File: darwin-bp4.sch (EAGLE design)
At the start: 21 parts, among them U1 MCP23008, U2 TCA9548A, U3 LP5012

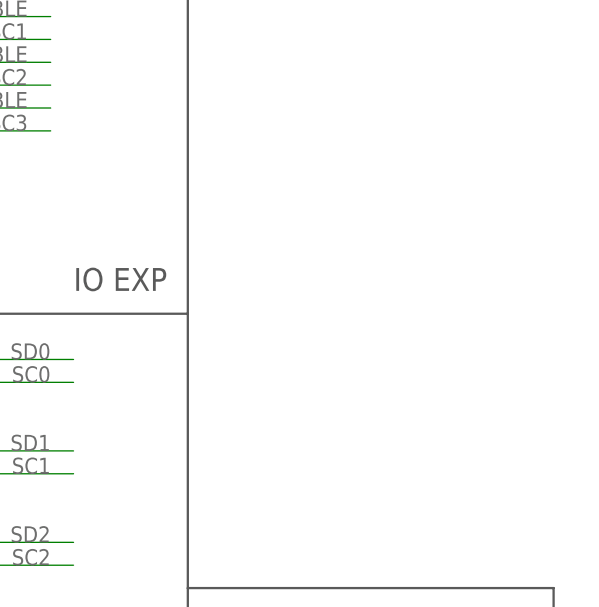
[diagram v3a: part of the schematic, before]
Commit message: Fixed power to LED controller, added pulldowns on hot swap detection pins, adjusted standoff holes.
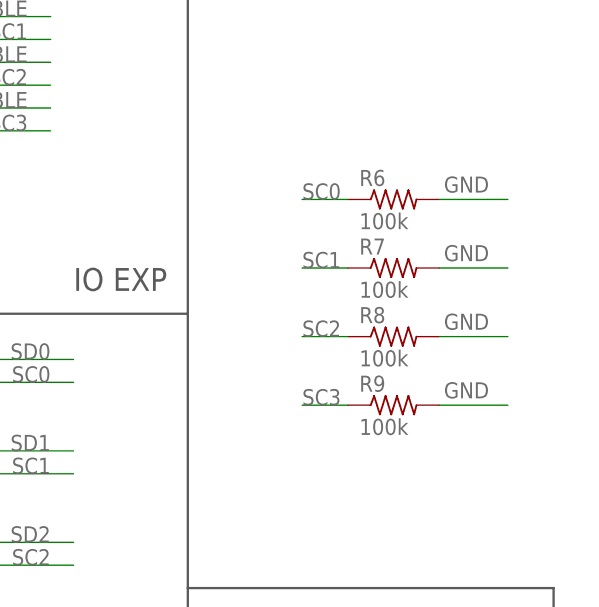
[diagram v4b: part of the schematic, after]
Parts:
- added R6, R7, R8, R9: 100k, rcl:R-US_R0603
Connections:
- net GND: now also R6.2, R7.2, R8.2, R9.2
- net SC0: now also R6.1
- net SC1: now also R7.1
- net SC2: now also R8.1
- net SC3: now also R9.1
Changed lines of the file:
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@@
 <?xml version="1.0" encoding="utf-8"?>
 <!DOCTYPE eagle SYSTEM "eagle.dtd">
-<eagle version="9.5.0">
+<eagle version="9.5.2">
 <drawing>
 <settings>
-<setting alwaysvectorfont="yes"/>
+<setting alwaysvectorfont="no"/>
 <setting verticaltext="up"/>
 </settings>
@@
 <part name="U$3" library="Conservify" library_urn="urn:adsk.eagle:library:11839183" deviceset="CLMVC-FKC-CGJJM569ABB7A343" device="" package3d_urn="urn:adsk.eagle:package:14540839/1"/>
 <part name="U$4" library="Conservify" library_urn="urn:adsk.eagle:library:11839183" deviceset="CLMVC-FKC-CGJJM569ABB7A343" device="" package3d_urn="urn:adsk.eagle:package:14540839/1"/>
+<part name="R6" library="rcl" library_urn="urn:adsk.eagle:library:334" deviceset="R-US_" device="R0603" package3d_urn="urn:adsk.eagle:package:23555/3" value="100k"/>
+<part name="R7" library="rcl" library_urn="urn:adsk.eagle:library:334" deviceset="R-US_" device="R0603" package3d_urn="urn:adsk.eagle:package:23555/3" value="100k"/>
+<part name="R8" library="rcl" library_urn="urn:adsk.eagle:library:334" deviceset="R-US_" device="R0603" package3d_urn="urn:adsk.eagle:package:23555/3" value="100k"/>
+<part name="R9" library="rcl" library_urn="urn:adsk.eagle:library:334" deviceset="R-US_" device="R0603" package3d_urn="urn:adsk.eagle:package:23555/3" value="100k"/>
 </parts>
 <sheets>
@@
 <instance part="U$3" gate="G$1" x="375.92" y="-134.62" smashed="yes" rot="R180"/>
 <instance part="U$4" gate="G$1" x="375.92" y="-152.4" smashed="yes" rot="R180"/>
+<instance part="R6" gate="G$1" x="368.3" y="-33.02" smashed="yes">
+<attribute name="NAME" x="364.49" y="-31.5214" size="1.778" layer="95"/>
+<attribute name="VALUE" x="364.49" y="-36.322" size="1.778" layer="96"/>
+</instance>
+<instance part="R7" gate="G$1" x="368.3" y="-40.64" smashed="yes">
+<attribute name="NAME" x="364.49" y="-39.1414" size="1.778" layer="95"/>
+<attribute name="VALUE" x="364.49" y="-43.942" size="1.778" layer="96"/>
+</instance>
+<instance part="R8" gate="G$1" x="368.3" y="-48.26" smashed="yes">
+<attribute name="NAME" x="364.49" y="-46.7614" size="1.778" layer="95"/>
+<attribute name="VALUE" x="364.49" y="-51.562" size="1.778" layer="96"/>
+</instance>
+<instance part="R9" gate="G$1" x="368.3" y="-55.88" smashed="yes">
+<attribute name="NAME" x="364.49" y="-54.3814" size="1.778" layer="95"/>
+<attribute name="VALUE" x="364.49" y="-59.182" size="1.778" layer="96"/>
+</instance>
 </instances>
 <busses>
@@
 <junction x="287.02" y="-132.08"/>
 </segment>
+<segment>
+<pinref part="R6" gate="G$1" pin="2"/>
+<wire x1="373.38" y1="-33.02" x2="381" y2="-33.02" width="0.1524" layer="91"/>
+<label x="373.888" y="-32.258" size="1.778" layer="95"/>
+</segment>
+<segment>
+<pinref part="R7" gate="G$1" pin="2"/>
+<wire x1="373.38" y1="-40.64" x2="381" y2="-40.64" width="0.1524" layer="91"/>
+<label x="373.888" y="-39.878" size="1.778" layer="95"/>
+</segment>
+<segment>
+<pinref part="R8" gate="G$1" pin="2"/>
+<wire x1="373.38" y1="-48.26" x2="381" y2="-48.26" width="0.1524" layer="91"/>
+<label x="373.888" y="-47.498" size="1.778" layer="95"/>
+</segment>
+<segment>
+<pinref part="R9" gate="G$1" pin="2"/>
+<wire x1="373.38" y1="-55.88" x2="381" y2="-55.88" width="0.1524" layer="91"/>
+<label x="373.888" y="-55.118" size="1.778" layer="95"/>
+</segment>
 </net>
 <net name="3V3" class="0">
@@
 <label x="327.66" y="-10.16" size="1.778" layer="95" align="bottom-right"/>
 </segment>
+<segment>
+<pinref part="R6" gate="G$1" pin="1"/>
+<wire x1="363.22" y1="-33.02" x2="358.14" y2="-33.02" width="0.1524" layer="91"/>
+<label x="358.14" y="-33.02" size="1.778" layer="95"/>
+</segment>
 </net>
 <net name="SC1" class="0">
@@
 <label x="327.66" y="-15.24" size="1.778" layer="95" align="bottom-right"/>
 </segment>
+<segment>
+<pinref part="R7" gate="G$1" pin="1"/>
+<wire x1="363.22" y1="-40.64" x2="358.14" y2="-40.64" width="0.1524" layer="91"/>
+<label x="358.14" y="-40.64" size="1.778" layer="95"/>
+</segment>
 </net>
 <net name="SD3" class="0">
@@
 <label x="327.66" y="-20.32" size="1.778" layer="95" align="bottom-right"/>
 </segment>
+<segment>
+<pinref part="R8" gate="G$1" pin="1"/>
+<wire x1="363.22" y1="-48.26" x2="358.14" y2="-48.26" width="0.1524" layer="91"/>
+<label x="358.14" y="-48.26" size="1.778" layer="95"/>
+</segment>
 </net>
 <net name="SD2" class="0">
@@
 <label x="327.66" y="-25.4" size="1.778" layer="95" align="bottom-right"/>
 </segment>
-</net>
+<segment>
+<pinref part="R9" gate="G$1" pin="1"/>
+<wire x1="363.22" y1="-55.88" x2="358.14" y2="-55.88" width="0.1524" layer="91"/>
+<label x="358.14" y="-55.88" size="1.778" layer="95"/>
+</segment>
+</net>

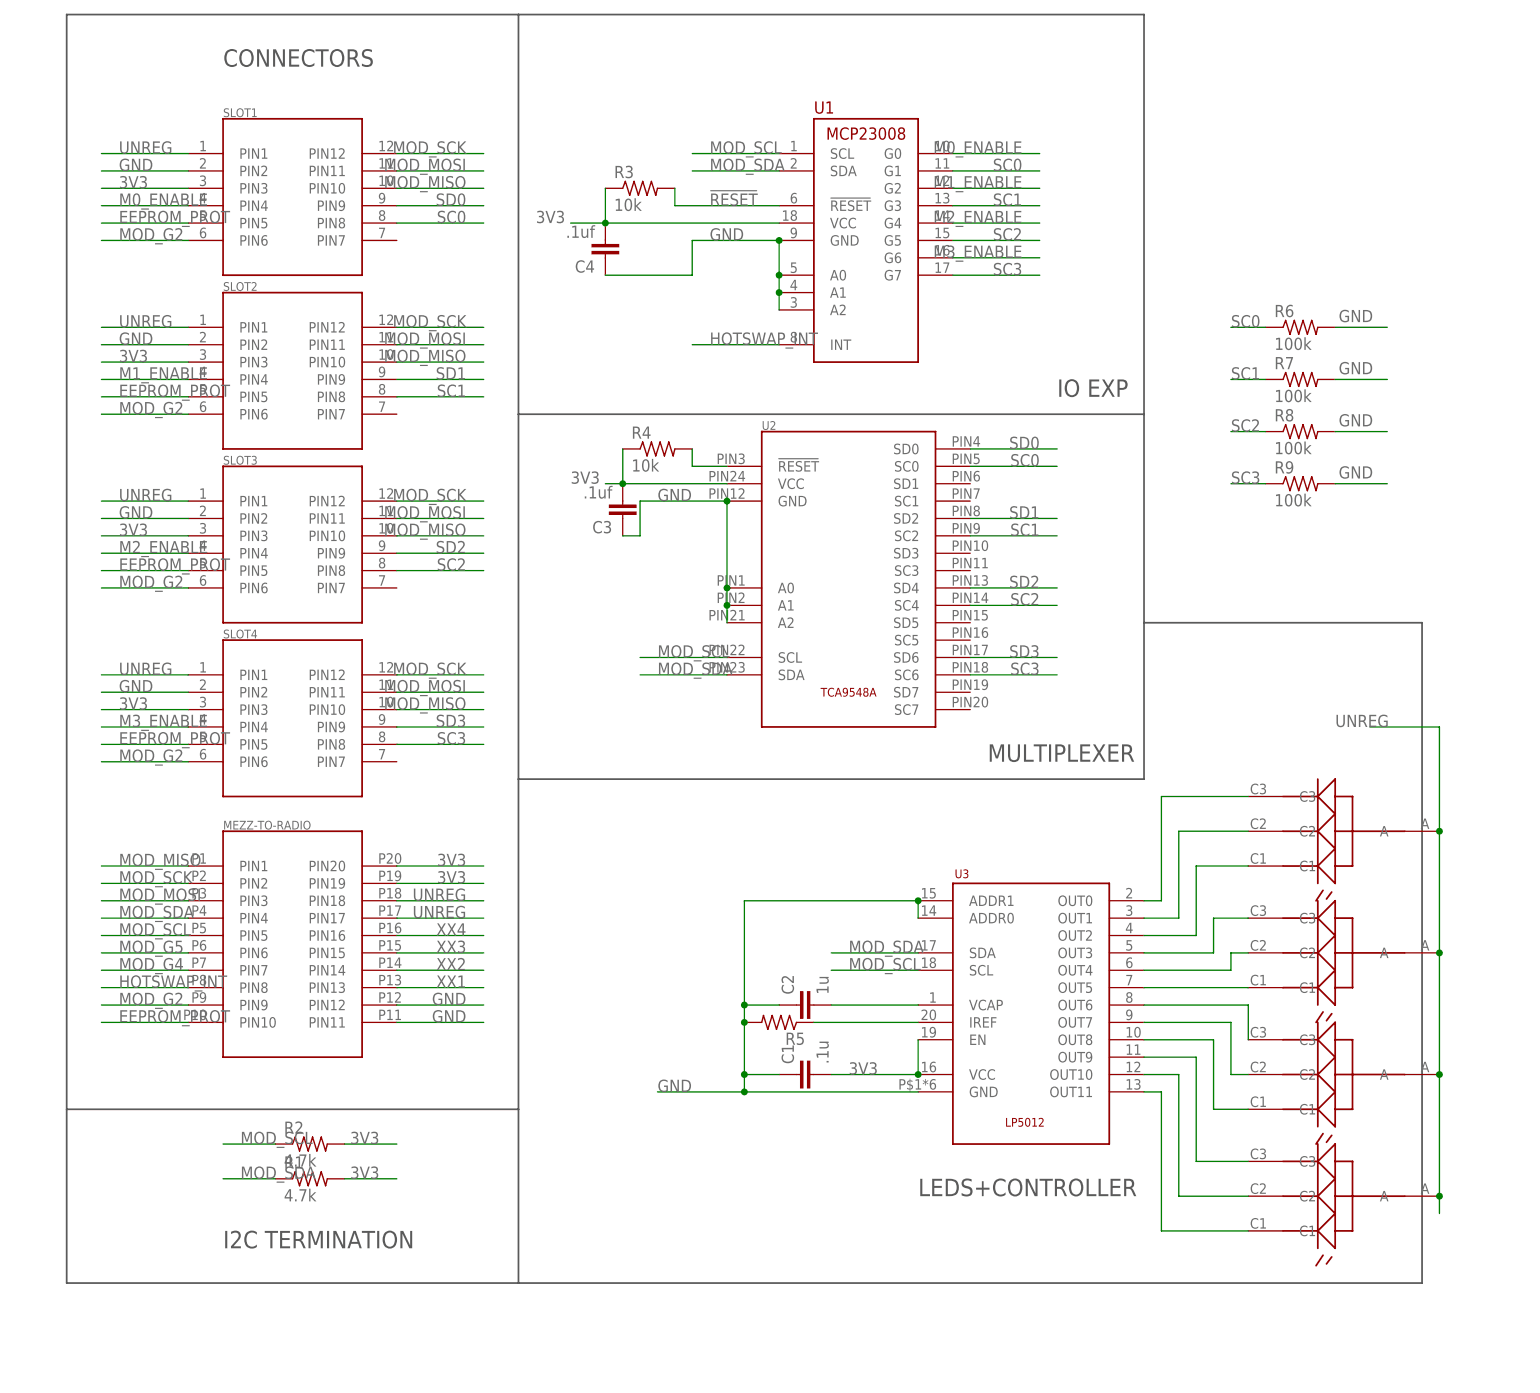
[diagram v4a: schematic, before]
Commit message: Cleaned up schematic and added PDF.
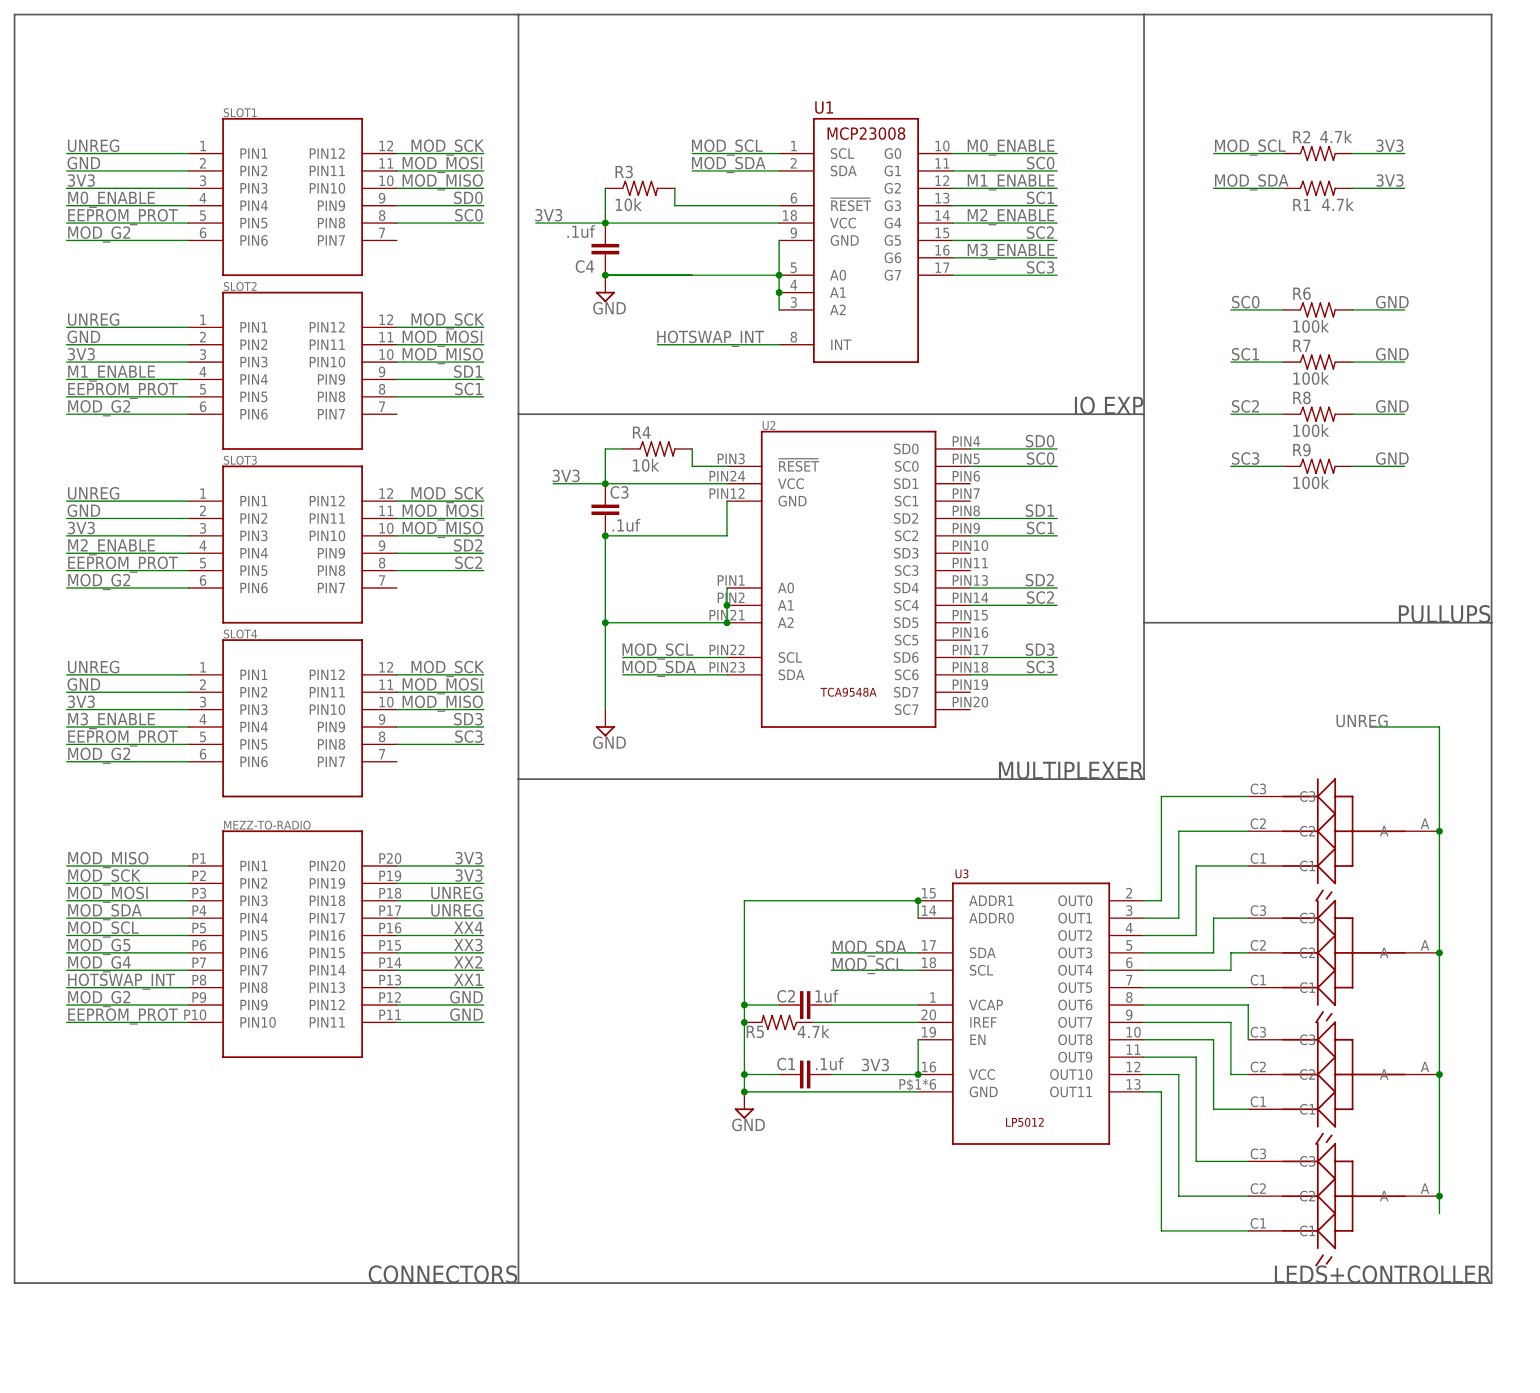
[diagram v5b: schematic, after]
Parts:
- C1: value .1u -> .1uf
- C2: value 1u -> 1uf
- R5: value (none) -> 4.7k
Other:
- note added: "PULLUPS"
- note removed: "I2C TERMINATION"
- moved on the sheet: C3, R1, R2, R6, R7, R8, R9

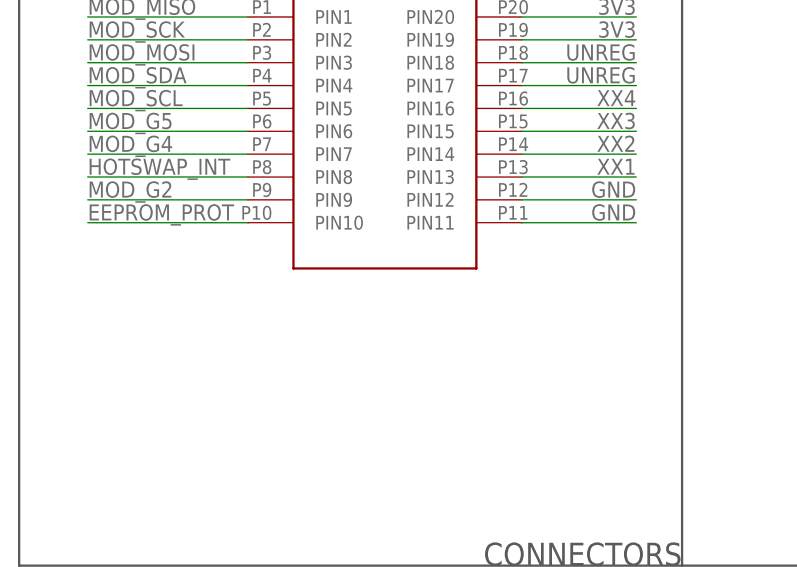
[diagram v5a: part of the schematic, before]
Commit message: Fixed updated connector footprint.
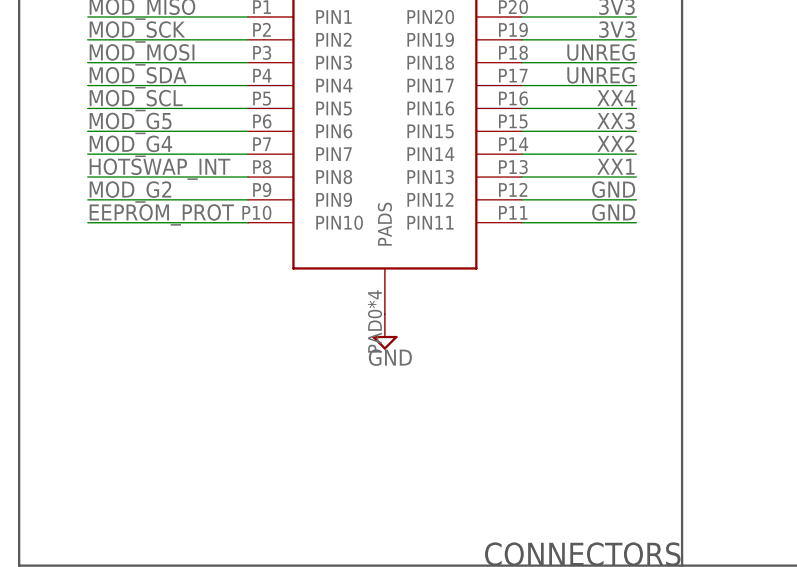
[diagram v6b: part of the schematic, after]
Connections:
- net GND: now also MEZZ-TO-RADIO.PADS
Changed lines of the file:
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@@
 </classes>
 <parts>
-<part name="MEZZ-TO-RADIO" library="Conservify" library_urn="urn:adsk.eagle:library:11839183" deviceset="M55-6102042R" device="7102(M)" package3d_urn="urn:adsk.eagle:package:11853513/2" value="M55-6102042R7102(M)"/>
+<part name="MEZZ-TO-RADIO" library="Conservify" library_urn="urn:adsk.eagle:library:11839183" deviceset="M55-6102042R" device="7102(M)" package3d_urn="urn:adsk.eagle:package:11853513/3" value="M55-6102042R7102(M)"/>
 <part name="U1" library="Conservify" library_urn="urn:adsk.eagle:library:11839183" deviceset="MCP23008" device="" package3d_urn="urn:adsk.eagle:package:11763623/2"/>
 <part name="SLOT1" library="Conservify" library_urn="urn:adsk.eagle:library:11839183" deviceset="2X6-HEADERS" device="DS" package3d_urn="urn:adsk.eagle:package:11839231/2" value="2X6-HEADERSDS"/>
@@
 <part name="SUPPLY2" library="supply2" library_urn="urn:adsk.eagle:library:372" deviceset="GND" device=""/>
 <part name="SUPPLY3" library="supply2" library_urn="urn:adsk.eagle:library:372" deviceset="GND" device=""/>
+<part name="SUPPLY4" library="supply2" library_urn="urn:adsk.eagle:library:372" deviceset="GND" device=""/>
 </parts>
 <sheets>
@@
 <attribute name="VALUE" x="285.115" y="-150.495" size="1.778" layer="96"/>
 </instance>
+<instance part="SUPPLY4" gate="GND" x="220.98" y="-147.32" smashed="yes">
+<attribute name="VALUE" x="219.075" y="-150.495" size="1.778" layer="96"/>
+</instance>
 </instances>
 <busses>
@@
 <label x="379.222" y="-53.086" size="1.778" layer="95"/>
 </segment>
-</net>
+<segment>
+<pinref part="MEZZ-TO-RADIO" gate="G$1" pin="PADS"/>
+<pinref part="SUPPLY4" gate="GND" pin="GND"/>
+</segment>
+</net>
